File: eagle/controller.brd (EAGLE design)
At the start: 100 x 80 mm, 27 parts, among them IC2 ATMEGA328, IC3 LT1490AIS8, IC4 LT1490AIS8, Q1 16MHz, X1 22-23-2031, X2 22-23-2021, X3 22-23-2021, X4 22-23-2021, X5 22-23-2101

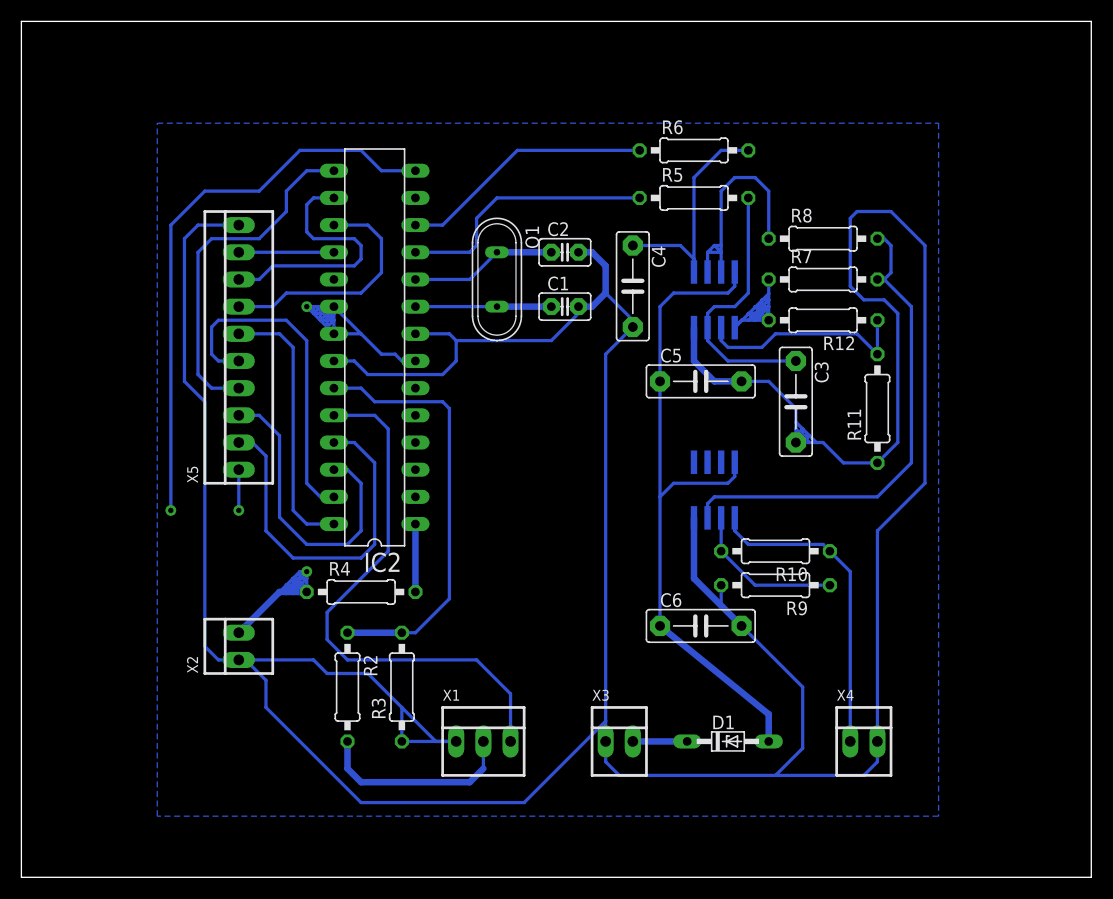
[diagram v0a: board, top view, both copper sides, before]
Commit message: Improve controller board design (Trace width, mounting holes, text)
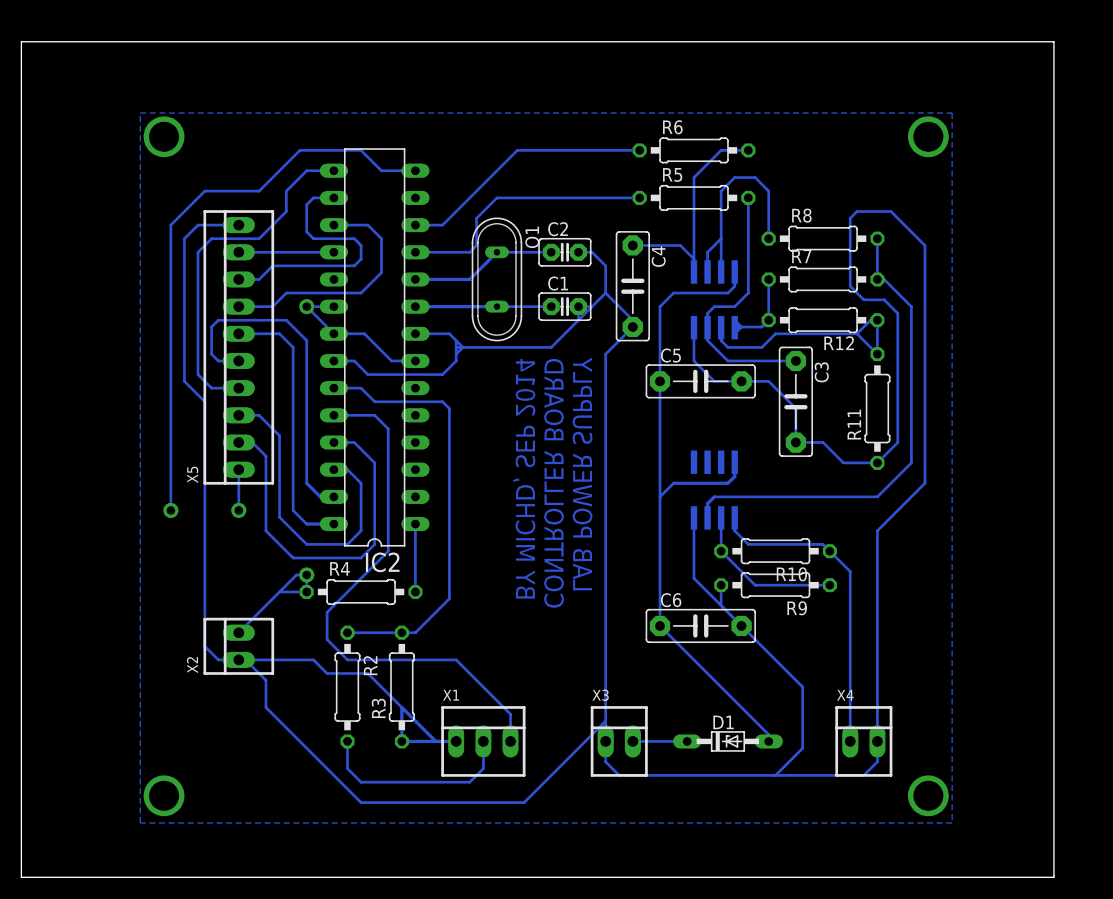
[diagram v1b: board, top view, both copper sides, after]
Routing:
- net N$4: track 63.3 -> 28.2 mm, vias 1 -> 2
- net N$5: track 26.4 -> 10.4 mm
- net GND: track 391.4 -> 385.9 mm
- net N$35: track 20.6 -> 23.0 mm
- net N$26: track 22.5 -> 20.6 mm
- net N$21: track 52.0 -> 50.2 mm
- net N$33: track 45.8 -> 44.6 mm
- net N$31: track 63.7 -> 63.1 mm
- added copper zone on layer 16, net N$35
- added copper zone on layer 16, net N$4
- added copper zone on layer 16, net N$5
- removed copper zone on layer 16, net N$6
- removed copper zone on layer 16, net N$9
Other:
- board size 100 x 80 mm -> 96.5 x 78.1 mm
- board text added: "LAB POWER SUPPLY CONTROLLER BOARD BY MICHD, SEP 2014"

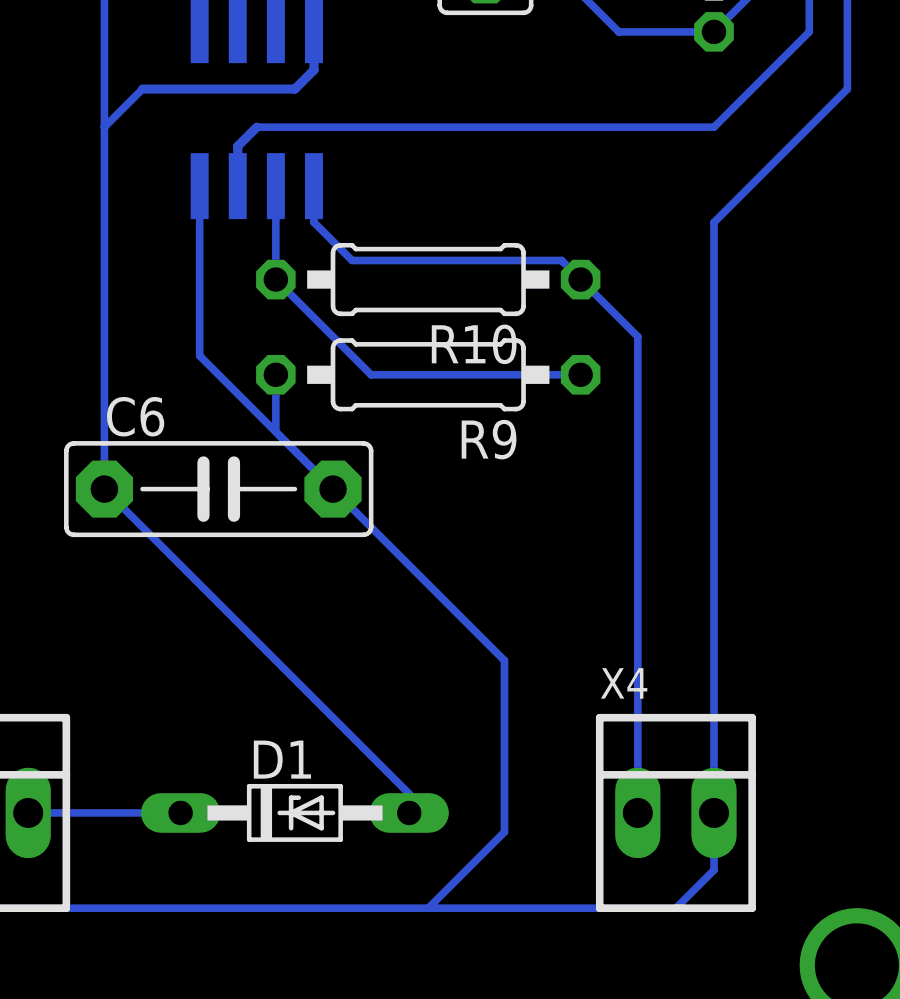
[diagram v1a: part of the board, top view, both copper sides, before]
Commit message: Correct mistakes in the controller opamp circuit
- Coarse voltage multiplier from 5->16.75V now from 5->30V
- Summing opamp was doubling voltage, now just voltage follower
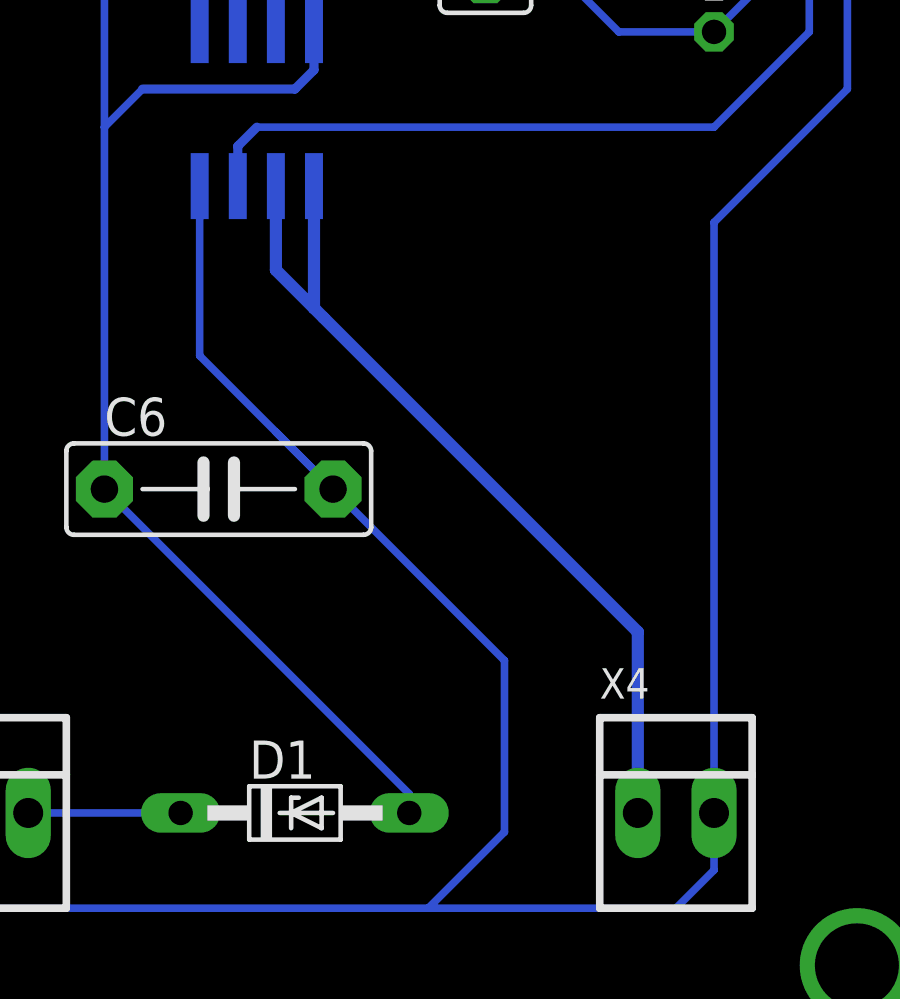
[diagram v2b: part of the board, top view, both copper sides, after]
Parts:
- removed R10, R9: 1k, rcl:0207/10
- R12: value 47k -> 100k
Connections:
- removed net N$37: IC4.1, R10.1, X4.1
- net GND: no longer R9.2
- net N$36: now also IC4.1, X4.1; no longer R10.2, R9.1
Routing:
- net N$37: track 29.5 -> 0.00 mm
- net N$36: track 14.6 -> 29.7 mm
- net GND: track 385.9 -> 384.0 mm
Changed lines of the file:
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@@
 <element name="R7" library="rcl" package="0207/10" value="47k" x="74.93" y="55.88"/>
 <element name="R8" library="rcl" package="0207/10" value="47k" x="74.93" y="59.69"/>
-<element name="R9" library="rcl" package="0207/10" value="1k" x="70.485" y="27.305" rot="R180"/>
-<element name="R10" library="rcl" package="0207/10" value="1k" x="70.485" y="30.48" rot="R180"/>
 <element name="R11" library="rcl" package="0207/10" value="20k" x="80.01" y="43.815" rot="R90"/>
-<element name="R12" library="rcl" package="0207/10" value="47k" x="74.93" y="52.07" rot="R180"/>
+<element name="R12" library="rcl" package="0207/10" value="100k" x="74.93" y="52.07" rot="R180"/>
 <element name="X4" library="con-molex" package="22-23-2021" value="22-23-2021" x="78.74" y="12.7">
 <attribute name="OC_NEWARK" value="25C3832" x="106.68" y="-30.48" size="1.778" layer="27" display="off"/>
@@
 <contactref element="IC3" pad="4"/>
 <contactref element="IC4" pad="4"/>
-<contactref element="R9" pad="2"/>
 <contactref element="R11" pad="1"/>
 <contactref element="X4" pad="2"/>
@@
 <wire x1="54.61" y1="54.61" x2="53.34" y2="53.34" width="0.254" layer="16"/>
 <wire x1="53.34" y1="53.34" x2="52.07" y2="53.34" width="0.254" layer="16"/>
-<wire x1="65.405" y1="27.305" x2="65.405" y2="25.4" width="0.254" layer="16"/>
 <wire x1="65.405" y1="25.4" x2="67.31" y2="23.495" width="0.254" layer="16"/>
 <wire x1="80.01" y1="38.735" x2="76.835" y2="38.735" width="0.254" layer="16"/>
@@
 </signal>
 <signal name="N$36">
-<contactref element="R9" pad="1"/>
 <contactref element="IC4" pad="2"/>
-<contactref element="R10" pad="2"/>
-<wire x1="65.405" y1="30.48" x2="65.405" y2="33.595" width="0.254" layer="16"/>
-<wire x1="75.565" y1="27.305" x2="68.58" y2="27.305" width="0.254" layer="16"/>
-<wire x1="68.58" y1="27.305" x2="65.405" y2="30.48" width="0.254" layer="16"/>
-</signal>
-<signal name="N$37">
-<contactref element="R10" pad="1"/>
+<contactref element="X4" pad="1"/>
 <contactref element="IC4" pad="1"/>
-<contactref element="X4" pad="1"/>
-<wire x1="66.675" y1="33.595" x2="66.675" y2="32.385" width="0.254" layer="16"/>
-<wire x1="66.675" y1="32.385" x2="67.945" y2="31.115" width="0.254" layer="16"/>
-<wire x1="67.945" y1="31.115" x2="74.93" y2="31.115" width="0.254" layer="16"/>
-<wire x1="74.93" y1="31.115" x2="75.565" y2="30.48" width="0.254" layer="16"/>
-<wire x1="77.47" y1="12.7" x2="77.47" y2="28.575" width="0.254" layer="16"/>
-<wire x1="77.47" y1="28.575" x2="75.565" y2="30.48" width="0.254" layer="16"/>
+<wire x1="66.675" y1="33.595" x2="66.675" y2="29.5275" width="0.4064" layer="16"/>
+<wire x1="66.675" y1="29.5275" x2="66.9925" y2="29.21" width="0.4064" layer="16"/>
+<wire x1="66.9925" y1="29.21" x2="77.47" y2="18.7325" width="0.4064" layer="16"/>
+<wire x1="77.47" y1="18.7325" x2="77.47" y2="12.7" width="0.4064" layer="16"/>
+<wire x1="65.405" y1="33.3375" x2="65.405" y2="30.7975" width="0.4064" layer="16"/>
+<wire x1="65.405" y1="30.7975" x2="66.675" y2="29.5275" width="0.4064" layer="16"/>
+<wire x1="65.405" y1="33.3375" x2="65.405" y2="33.595" width="0" layer="19" extent="16-16"/>
 </signal>
 <signal name="N$35">

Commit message: Correct another mistake in controller board
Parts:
- R2: value 680k -> 68k
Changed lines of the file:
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@@
 <attribute name="OC_FARNELL" value="unknown" x="52.07" y="81.28" size="1.778" layer="27" rot="R90" display="off"/>
 </element>
-<element name="R2" library="rcl" package="0207/10" value="680k" x="30.48" y="17.78" rot="R270"/>
+<element name="R2" library="rcl" package="0207/10" value="68k" x="30.48" y="17.78" rot="R270"/>
 <element name="R3" library="rcl" package="0207/10" value="10k" x="35.56" y="17.78" rot="R90"/>
 <element name="Q1" library="special" package="QS" value="16MHz" x="44.45" y="55.88" rot="R270"/>
